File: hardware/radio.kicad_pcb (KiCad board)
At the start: 2 copper layers, 65 x 56 mm, 89 parts, among them J1 JCLK, U1 G144A12, U3V3t1V8 NCP1117ST18T3G, U5V0t3V3 NCP1117ST33T3G

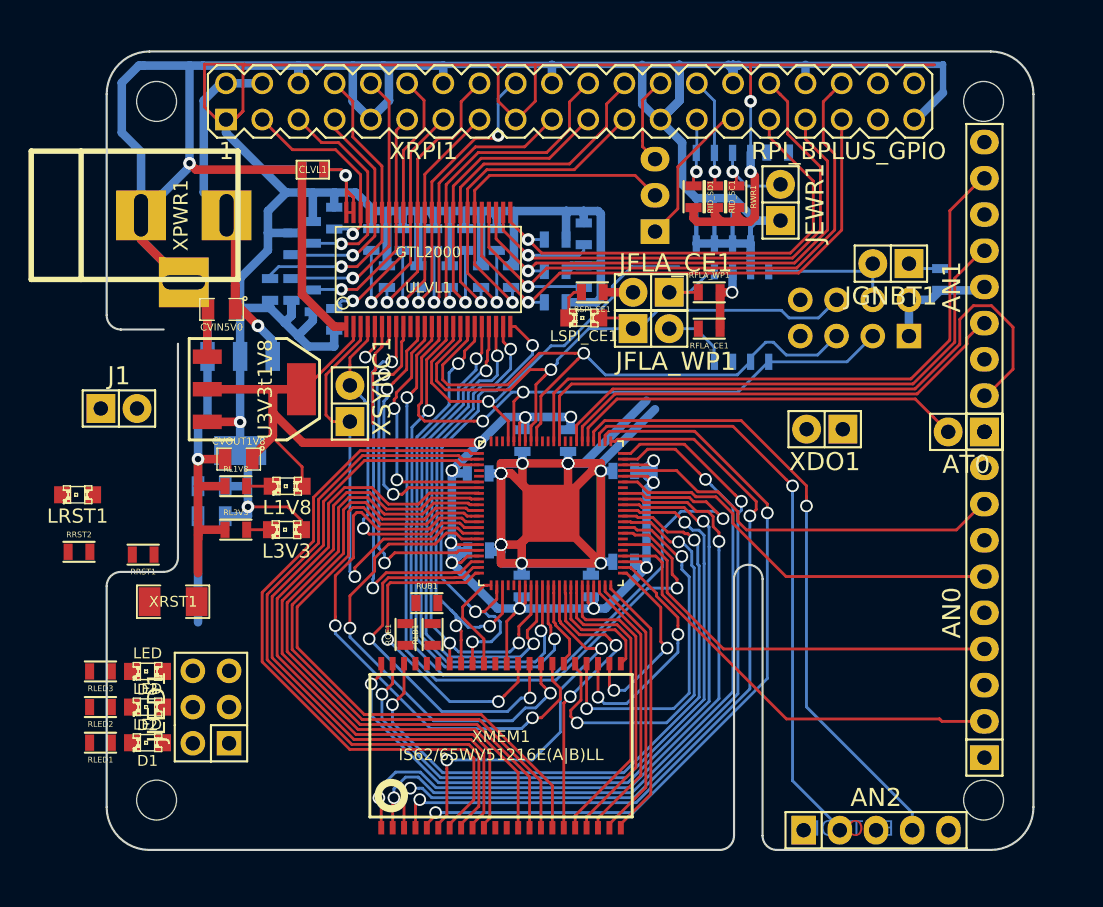
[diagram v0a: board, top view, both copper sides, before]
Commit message: Adding the UART header.
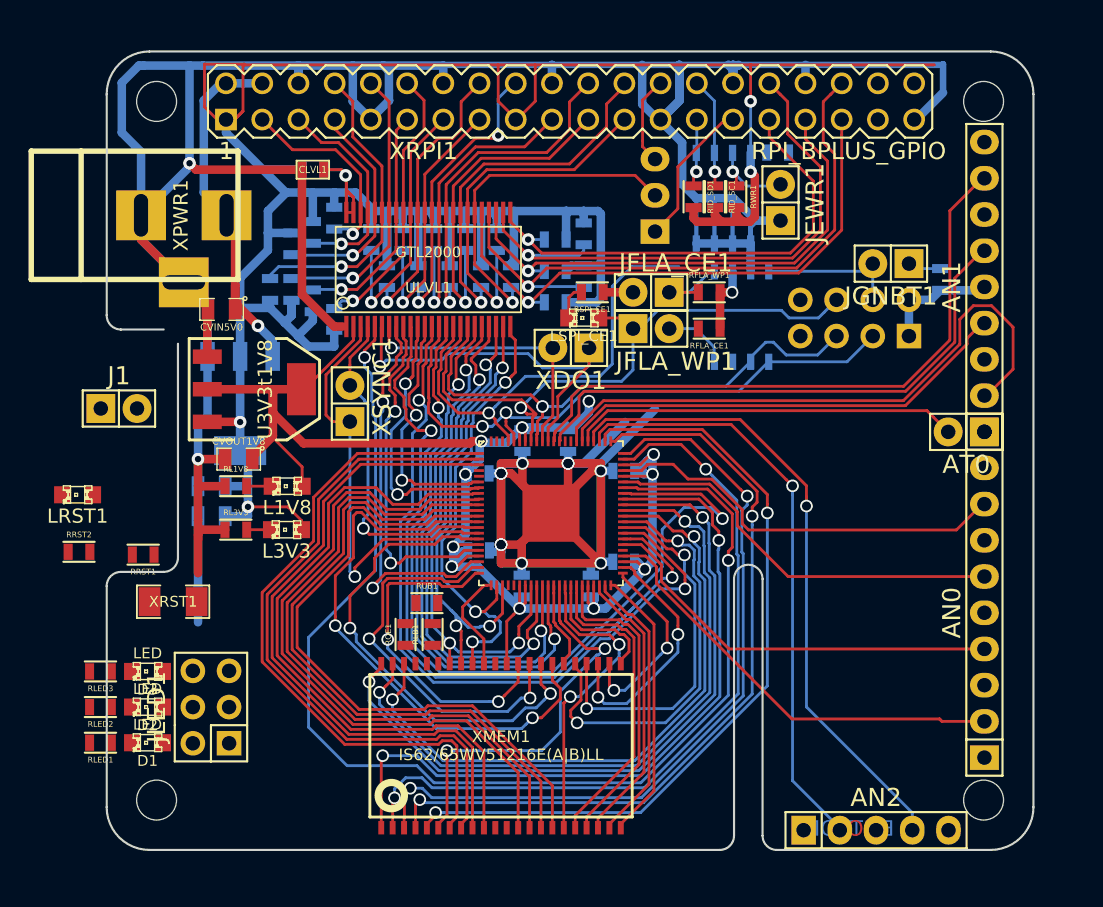
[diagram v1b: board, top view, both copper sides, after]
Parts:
- moved XDO1 18.7 mm to (49.5, 38.1)
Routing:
- net REFCLK1_L: track 2.42 -> 85.5 mm, vias 1 -> 2
- net REFCLK2_L: track 0.00 -> 55.9 mm, vias 0 -> 2
- net /TXDO_L: track 7.07 -> 27.4 mm, vias 0 -> 1
- net /RXDO_L: track 1.16 -> 19.8 mm, vias 0 -> 1
- net SPI_CLK: track 43.4 -> 38.2 mm
- net SPI_MISO: track 40.3 -> 42.6 mm
- net GND: track 367.2 -> 365.1 mm
- net SPI_MOSI: track 45.0 -> 43.1 mm
- net GPIO_06_L: track 34.6 -> 32.8 mm
- net /GPIO_24_L: track 52.4 -> 54.2 mm
- net /ADDR4: track 50.0 -> 51.5 mm
- net /ADDR2: track 53.1 -> 54.5 mm
- net SPI_~CE: track 44.3 -> 45.6 mm
- net /DATA0: track 49.3 -> 48.2 mm
- net VDD: track 129.2 -> 128.1 mm
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
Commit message: All traces routed I think.
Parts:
- RRST1: moved to B.Cu
- moved J1 48.9 mm to (65.9, 50.9), turned to 270 degrees
- moved RRST1 26.1 mm to (43.8, 43.1), turned to 0 degrees
- moved LRST1 15.7 mm to (29.6, 54.0)
- moved RRST2 11.1 mm to (26.0, 54.0)
- moved JLED1 3.37 mm to (27.6, 62.9)
- moved D1 3.22 mm to (23.0, 65.4)
- moved RLED1 3.22 mm to (19.7, 65.4)
- moved D2 3.22 mm to (23.0, 62.9)
- moved D3 3.22 mm to (23.0, 60.4)
- moved RLED2 3.22 mm to (19.7, 62.9)
- moved RLED3 3.22 mm to (19.7, 60.4)
- moved XRST1 1.02 mm to (20.6, 56.1), turned to 180 degrees
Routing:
- net GND: track 365.1 -> 490.2 mm
- net VDD: track 128.1 -> 244.2 mm
- net RST: track 0.00 -> 53.2 mm, vias 0 -> 1
- net /ADDRN18: track 6.13 -> 32.4 mm, vias 0 -> 2
- net /~WE: track 21.8 -> 46.1 mm, vias 2 -> 3
- net /~CE: track 27.9 -> 47.8 mm
- net SPI_MISO: track 42.6 -> 55.6 mm
- net REFCLK2_L: track 55.9 -> 67.1 mm
- net /DATA7: track 46.1 -> 40.3 mm
- net /DATA6: track 46.5 -> 41.2 mm
- net /DATA5: track 46.9 -> 41.6 mm
- net /DATA4: track 47.3 -> 42.2 mm
- net /717.ao: track 45.1 -> 50.0 mm
- net Net-(RUB1-Pad2): track 0.00 -> 4.56 mm
- net /DATA3: track 46.8 -> 42.4 mm
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- added copper zone on B.Cu, net GND
- added copper zone on F.Cu, net VDD

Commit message: Lots of small fixes.
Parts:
- moved AN2 5.10 mm to (70.9, 66.8)
- moved ROE1 3.12 mm to (39.4, 55.5), turned to 180 degrees
- moved RUB1 2.25 mm to (39.4, 58.2)
- moved J1 1.60 mm to (65.9, 49.3)
- moved RLB1 1.41 mm to (39.4, 56.9), turned to 180 degrees
- moved XMEM1 0.33 mm to (44.6, 65.7)
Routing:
- net GND: track 490.2 -> 375.4 mm, vias 12 -> 14
- net (no net): track 0.00 -> 81.8 mm
- net VDD: track 244.2 -> 200.1 mm, vias 12 -> 13
- net +3.3V: track 222.0 -> 209.5 mm
- net /GPIO_25_L: track 60.8 -> 54.1 mm
- net /ADDR8: track 29.4 -> 22.8 mm
- net /ADDR9: track 23.1 -> 17.4 mm
- net SPI_~CE: track 48.5 -> 43.4 mm
- net /ADDR7: track 46.8 -> 42.0 mm
- net /ADDR6: track 49.2 -> 44.5 mm
- net /SDA1_L: track 32.8 -> 28.4 mm
- net /ADDR5: track 51.3 -> 47.0 mm
- net /717.ao: track 50.0 -> 45.9 mm
- net GPIO_06_L: track 32.8 -> 36.8 mm
- net SPI_CLK: track 40.9 -> 36.9 mm
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
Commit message: Making clearance 0.15**24** and trace width 0.15**24**.
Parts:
- moved XRST1 1.94 mm to (22.5, 56.5)
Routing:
- net GND: track 375.4 -> 406.6 mm, vias 14 -> 19
- net VDD: track 200.1 -> 203.2 mm
- net SPI_MISO: track 52.7 -> 55.6 mm
- net /GPIO_25_L: track 54.1 -> 56.5 mm
- net GPIO_06_L: track 36.8 -> 34.5 mm
- net /117.ai: track 33.7 -> 31.5 mm
- net /117.ao: track 31.8 -> 29.7 mm
- net /ADDR2: track 54.7 -> 53.0 mm
- net /ADDR1: track 56.3 -> 54.7 mm
- net RST: track 52.1 -> 50.7 mm
- net SPI_MOSI: track 44.0 -> 42.6 mm
- net /ADDR0: track 57.6 -> 56.4 mm
- net /ADDR3: track 53.2 -> 52.5 mm
- net REFCLK2_L: track 63.9 -> 63.2 mm
- net GPIO_19_L: track 38.8 -> 38.2 mm
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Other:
- net class Analog: clearance 0.15 -> 0.1524; trace_width 0.2 -> 0.1524
- net class Default: clearance 0.15 -> 0.1524; trace_width 0.2 -> 0.1524
- net class Memory: clearance 0.15 -> 0.1524; trace_width 0.2 -> 0.1524
- net class PWR: clearance 0.15 -> 0.1524
- rule trace_clearance: 0.15 -> 0.1524
- rule trace_min: 0.15 -> 0.1524

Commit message: More work.
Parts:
- moved J1 0.69 mm to (66.0, 48.6)
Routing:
- net (no net): track 81.6 -> 0.00 mm
- net +3.3V: track 209.5 -> 186.1 mm
- net VDD: track 203.2 -> 209.1 mm
- net GND: track 406.6 -> 404.1 mm, vias 19 -> 20
- net SPI_MISO: track 55.6 -> 53.3 mm
- net /DATA8: track 35.7 -> 37.7 mm
- net /ADDR3: track 52.5 -> 54.4 mm
- net /DATA6: track 42.0 -> 43.4 mm
- net /DATA7: track 41.8 -> 43.1 mm
- net SPI_MOSI: track 42.6 -> 41.4 mm
- net /DATA5: track 42.5 -> 43.7 mm
- net /DATA4: track 42.9 -> 44.0 mm
- net /DATA3: track 42.8 -> 43.9 mm
- net /GPIO_24_L: track 53.7 -> 54.7 mm
- net /DATA2: track 44.5 -> 45.5 mm
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
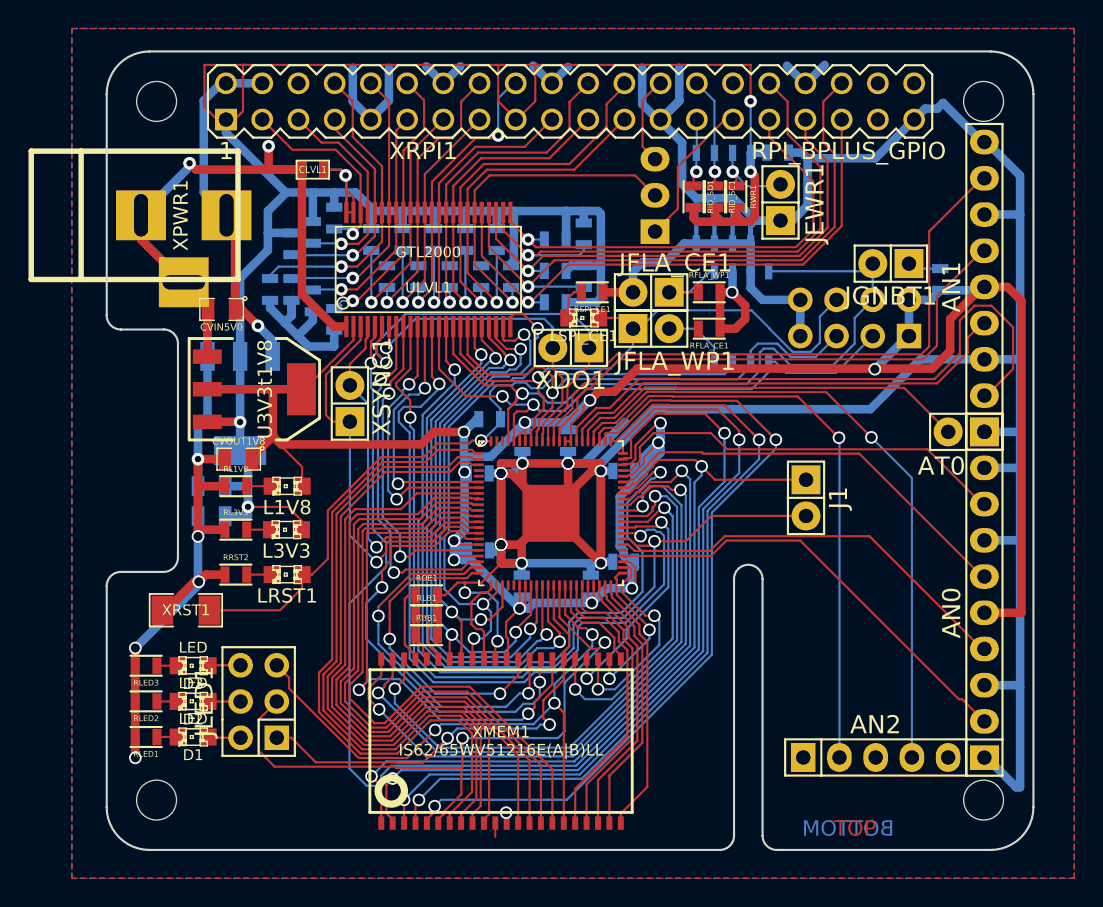
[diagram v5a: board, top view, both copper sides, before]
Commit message: 4 layer design.
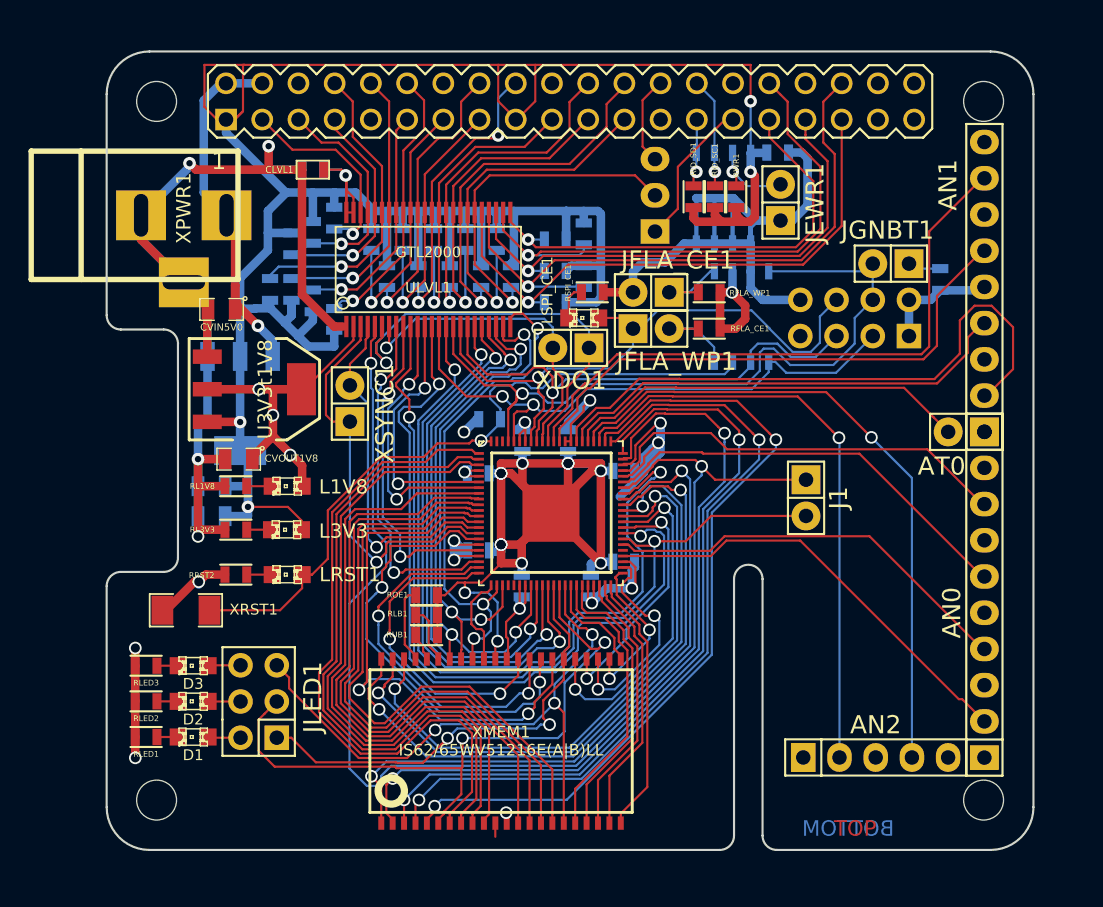
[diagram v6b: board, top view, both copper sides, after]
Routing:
- net GND: track 404.1 -> 221.9 mm
- net VDD: track 209.1 -> 107.8 mm, vias 13 -> 15
- net +3.3V: track 186.1 -> 203.8 mm
- net /JFLA_CE: track 4.72 -> 6.94 mm
- added copper zone on In1.Cu, net GND
- added copper zone on In2.Cu, net VDD
- removed copper zone on B.Cu, net GND
- removed copper zone on F.Cu, net VDD
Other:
- copper layers 2 -> 4
- board text added: "AN0"
- board text added: "AN1"
- board text added: "AN2"
- board text added: "ATO"
- board text added: "J1"
- board text added: "JLED1"
- board text added: "XDO1"
- board text added: "XSPI1"
- board text added: "XSYNC1"

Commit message: More 4 layer work.
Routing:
- net GND: track 221.9 -> 447.5 mm
- net VDD: track 107.8 -> 232.0 mm, vias 15 -> 17
- net +3.3V: track 203.8 -> 202.6 mm
- net /DATA8: track 37.7 -> 38.5 mm

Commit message: More optimisation.
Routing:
- net GND: track 447.5 -> 412.5 mm
- net VDD: track 232.0 -> 224.3 mm, vias 17 -> 15
- net /ADDR3: track 54.4 -> 53.3 mm
